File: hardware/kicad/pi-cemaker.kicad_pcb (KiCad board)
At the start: 4 copper layers, 85 x 56 mm, 4 parts

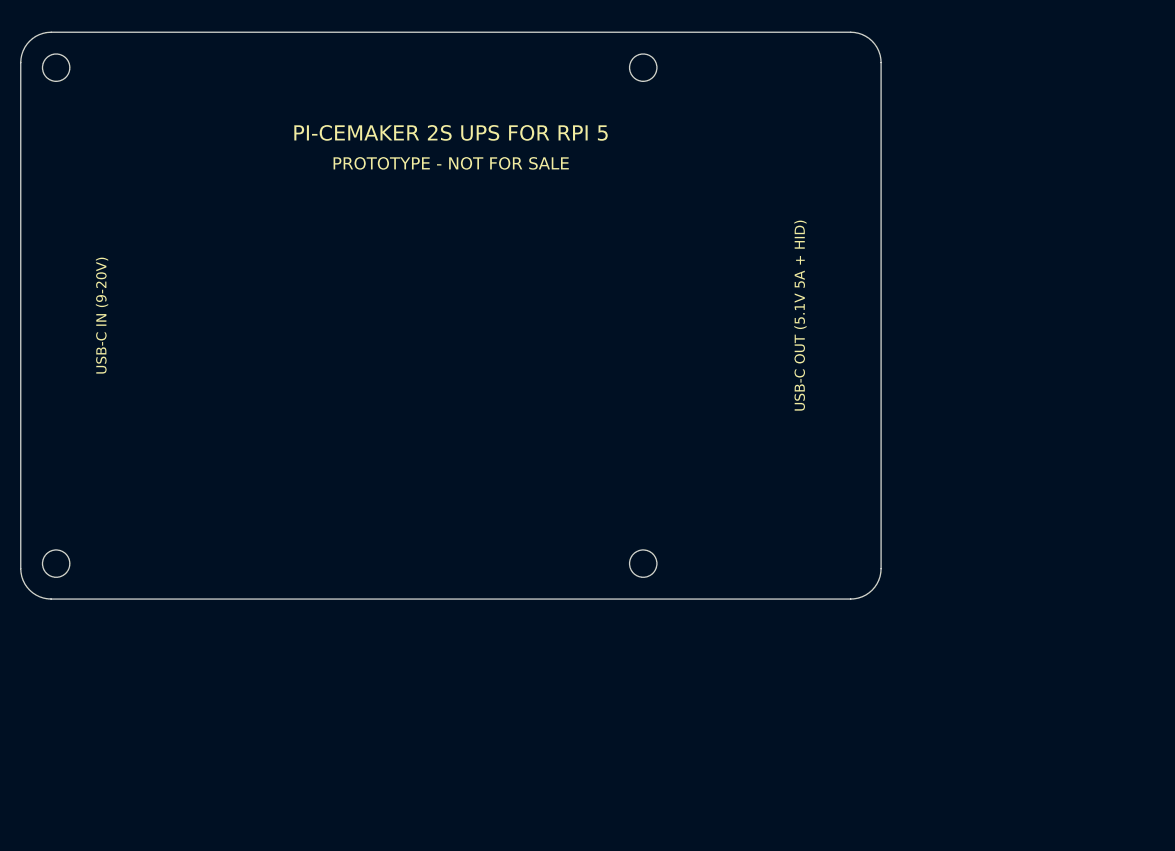
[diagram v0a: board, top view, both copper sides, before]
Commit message: hardware: draft Lite board generated from design.py (ERC clean, PCB unrouted/unreviewed)
Schematic (110 parts, ERC 0 violations), hand-built BQ25792 footprint,
placed + autorouted draft PCB (38 connections unrouted), draft BOM and a
decision log with a reversal path for each guess. No fab files produced.

Co-Authored-By: Claude Sonnet 5.5 <noreply@anthropic.com>
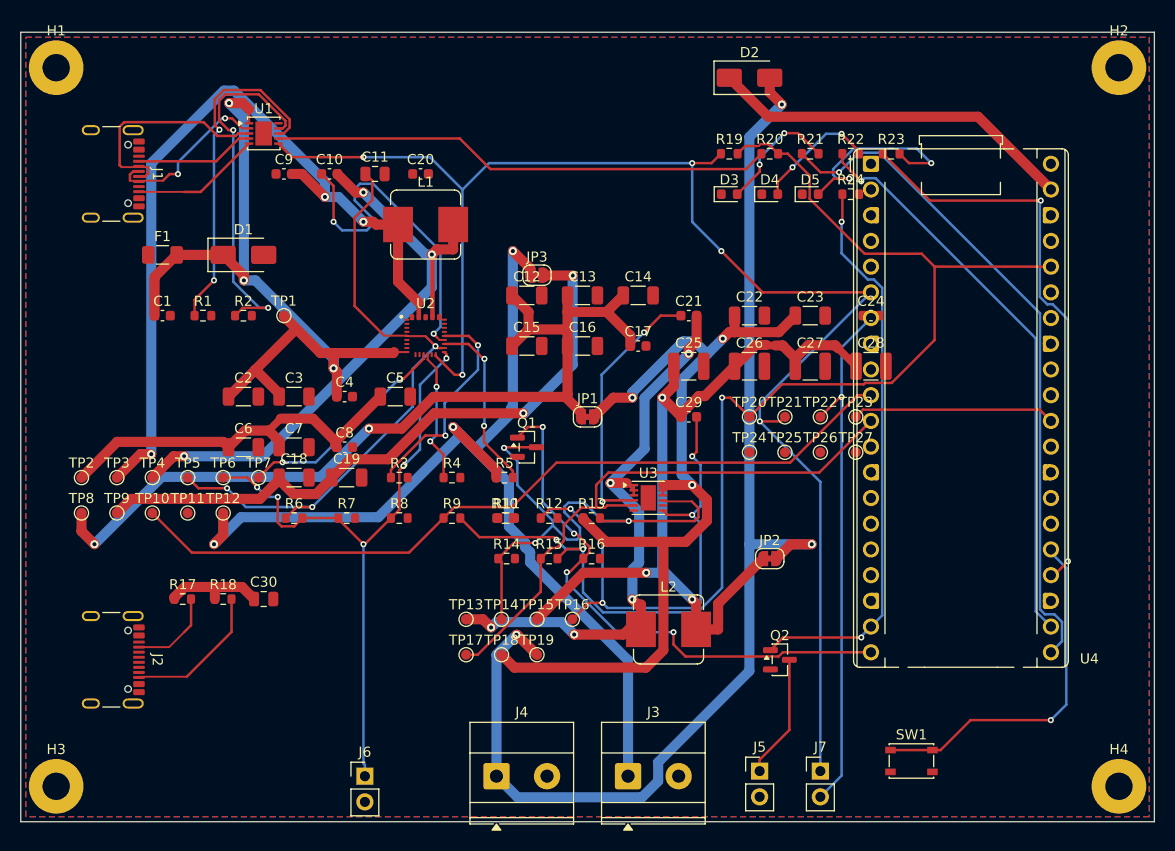
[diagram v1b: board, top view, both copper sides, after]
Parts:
- removed ? (x4): , MountingHole:MountingHole_2.7mm_M2.5
- added C1: 1uF 25V, C_0603_1608Metric, F.Cu at (14.0, 28.0)
- added C10: 47nF 25V, C_0603_1608Metric, F.Cu at (30.5, 14.0)
- added C11: 4.7uF 10V, C_0805_2012Metric, F.Cu at (35.0, 14.0)
- added C12: 10uF 25V, C_1206_3216Metric, F.Cu at (50.0, 26.0)
- added C13: 10uF 25V, C_1206_3216Metric, F.Cu at (55.5, 26.0)
- added C14: 10uF 25V, C_1206_3216Metric, F.Cu at (61.0, 26.0)
- added C15: 10uF 25V, C_1206_3216Metric, F.Cu at (50.0, 31.0)
- added C16: 10uF 25V, C_1206_3216Metric, F.Cu at (55.5, 31.0)
- added C17: 100nF 25V, C_0603_1608Metric, F.Cu at (61.0, 31.0)
- added C18: 10uF 16V, C_1206_3216Metric, F.Cu at (27.0, 44.0)
- added C19: 10uF 16V, C_1206_3216Metric, F.Cu at (32.2, 44.0)
- added C2: 10uF 25V, C_1206_3216Metric, F.Cu at (22.0, 36.0)
- added C20: 1nF 50V, C_0603_1608Metric, F.Cu at (39.5, 14.0)
- added C21: 100nF 16V, C_0603_1608Metric, F.Cu at (66.0, 28.0)
- added C22: 10uF 25V, C_1206_3216Metric, F.Cu at (72.0, 28.0)
- added C23: 10uF 25V, C_1206_3216Metric, F.Cu at (78.0, 28.0)
- added C24: 100nF 25V, C_0603_1608Metric, F.Cu at (84.0, 28.0)
- added C25: 33uF 16V, C_1210_3225Metric, F.Cu at (66.0, 33.0)
- added C26: 33uF 16V, C_1210_3225Metric, F.Cu at (72.0, 33.0)
- added C27: 33uF 16V (spare), C_1210_3225Metric, F.Cu at (78.0, 33.0)
- added C28: 33uF 16V (spare), C_1210_3225Metric, F.Cu at (84.0, 33.0)
- added C29: 33pF (CFF), C_0603_1608Metric, F.Cu at (66.0, 38.0)
- added C3: 10uF 25V, C_1206_3216Metric, F.Cu at (27.0, 36.0)
- added C30: 10uF 10V, C_0805_2012Metric, F.Cu at (24.0, 56.0)
- added C4: 100nF 25V, C_0603_1608Metric, F.Cu at (32.0, 36.0)
- added C5: 10uF 25V, C_1206_3216Metric, F.Cu at (37.0, 36.0)
- added C6: 10uF 25V, C_1206_3216Metric, F.Cu at (22.0, 41.0)
- added C7: 10uF 25V, C_1206_3216Metric, F.Cu at (27.0, 41.0)
- added C8: 100nF 25V, C_0603_1608Metric, F.Cu at (32.0, 41.0)
- added C9: 47nF 25V, C_0603_1608Metric, F.Cu at (26.0, 14.0)
- added D1: SMAJ13A, D_SMA, F.Cu at (22.0, 22.0)
- added D2: SS34, D_SMA, F.Cu at (72.0, 4.50)
- added D3: green, LED_0603_1608Metric, F.Cu at (70.0, 16.0)
- added D4: amber, LED_0603_1608Metric, F.Cu at (74.0, 16.0)
- added D5: red, LED_0603_1608Metric, F.Cu at (78.0, 16.0)
- added F1: 3.15A or 0R (fit one), Fuse_1206_3216Metric, F.Cu at (14.0, 22.0)
- added H1: M2.5, MountingHole_2.7mm_M2.5_Pad, F.Cu at (3.50, 3.50)
- added H2: M2.5, MountingHole_2.7mm_M2.5_Pad, F.Cu at (108.5, 3.50)
- added H3: M2.5, MountingHole_2.7mm_M2.5_Pad, F.Cu at (3.50, 74.5)
- added H4: M2.5, MountingHole_2.7mm_M2.5_Pad, F.Cu at (108.5, 74.5)
- added J1: USB-C in (PD sink), USB_C_Receptacle_GCT_USB4105-xx-A_16P_TopMnt_Horizontal, F.Cu at (8.00, 14.0)
- added J2: USB-C out to Pi 5 (power only), USB_C_Receptacle_GCT_USB4105-xx-A_16P_TopMnt_Horizontal, F.Cu at (8.00, 62.0)
- added J3: PACK+ / PACK- (off-board 2S BMS), TerminalBlock_Phoenix_MKDS-1,5-2_1x02_P5.00mm_Horizontal, F.Cu at (60.0, 73.5)
- added J4: 5V OUT / GND, TerminalBlock_Phoenix_MKDS-1,5-2_1x02_P5.00mm_Horizontal, F.Cu at (47.0, 73.5)
- added J5: To Pi 5 J2 power button, PinHeader_1x02_P2.54mm_Vertical, F.Cu at (73.0, 73.0)
- added J6: NTC (optional), PinHeader_1x02_P2.54mm_Vertical, F.Cu at (34.0, 73.5)
- added J7: I2C expansion (3V3 SDA), PinHeader_1x02_P2.54mm_Vertical, F.Cu at (79.0, 73.0)
- added JP1: VSYS link, SolderJumper-2_P1.3mm_Bridged_RoundedPad1.0x1.5mm, F.Cu at (56.0, 38.0)
- added JP2: 5V link, SolderJumper-2_P1.3mm_Bridged_RoundedPad1.0x1.5mm, F.Cu at (74.0, 52.0)
- added JP3: PACK link, SolderJumper-2_P1.3mm_Bridged_RoundedPad1.0x1.5mm, F.Cu at (51.0, 24.0)
- added L1: 1uH >=8A sat, L_Bourns_SRP7028A_7.3x6.6mm, F.Cu at (40.0, 19.0)
- added L2: 4.7uH >=8A sat, L_Bourns_SRP7028A_7.3x6.6mm, F.Cu at (64.0, 59.0)
- added Q1: 2N7002, SOT-23, F.Cu at (50.0, 41.0)
- added Q2: 2N7002, SOT-23, F.Cu at (75.0, 62.0)
- added R1: 10k (12 V), R_0603_1608Metric, F.Cu at (18.0, 28.0)
- added R10: 10k, R_0603_1608Metric, F.Cu at (47.8, 48.0)
- added R11: 102k (FBT), R_0603_1608Metric, F.Cu at (48.0, 48.0)
- added R12: 19.1k (FBB), R_0603_1608Metric, F.Cu at (52.2, 48.0)
- added R13: 62k (ENT), R_0603_1608Metric, F.Cu at (56.4, 48.0)
- added R14: 21.5k (ENB), R_0603_1608Metric, F.Cu at (48.0, 52.0)
- added R15: 10k, R_0603_1608Metric, F.Cu at (52.2, 52.0)
- added R16: 100k (gate pull-down), R_0603_1608Metric, F.Cu at (56.4, 52.0)
- added R17: 10k (Rp, 3 A), R_0603_1608Metric, F.Cu at (16.0, 56.0)
- added R18: 10k (Rp, 3 A), R_0603_1608Metric, F.Cu at (20.0, 56.0)
- added R19: 10k, R_0603_1608Metric, F.Cu at (70.0, 12.0)
- added R2: 22.6k (3 A), R_0603_1608Metric, F.Cu at (22.0, 28.0)
- added R20: 10k, R_0603_1608Metric, F.Cu at (74.0, 12.0)
- added R21: 1k, R_0603_1608Metric, F.Cu at (78.0, 12.0)
- added R22: 1k, R_0603_1608Metric, F.Cu at (82.0, 12.0)
- added R23: 1k, R_0603_1608Metric, F.Cu at (86.0, 12.0)
- added R24: 100k (gate pull-down), R_0603_1608Metric, F.Cu at (82.0, 16.0)
- added R3: 6.04k 1% (2S,1.5MHz), R_0603_1608Metric, F.Cu at (37.4, 44.0)
- added R4: 10k (CE low = charge on), R_0603_1608Metric, F.Cu at (42.6, 44.0)
- added R5: 100R, R_0603_1608Metric, F.Cu at (47.8, 44.0)
- added R6: 5.24k (RT1), R_0603_1608Metric, F.Cu at (27.0, 48.0)
- added R7: 30.31k (RT2), R_0603_1608Metric, F.Cu at (32.2, 48.0)
- added R8: 10k fixed NTC stand-in, R_0603_1608Metric, F.Cu at (37.4, 48.0)
- added R9: 10k, R_0603_1608Metric, F.Cu at (42.6, 48.0)
- added SW1: USER, SW_SPST_PTS810, F.Cu at (88.0, 72.0)
- added TP1: VBUS, TestPoint_Pad_D1.0mm, F.Cu at (26.0, 28.0)
- added TP10: STAT, TestPoint_Pad_D1.0mm, F.Cu at (13.0, 47.5)
- added TP11: INT, TestPoint_Pad_D1.0mm, F.Cu at (16.5, 47.5)
- added TP12: PACK_P, TestPoint_Pad_D1.0mm, F.Cu at (20.0, 47.5)
- added TP13: SW_B, TestPoint_Pad_D1.0mm, F.Cu at (44.0, 58.0)
- added TP14: EN_B, TestPoint_Pad_D1.0mm, F.Cu at (47.5, 58.0)
- added TP15: V5_B, TestPoint_Pad_D1.0mm, F.Cu at (51.0, 58.0)
- added TP16: FB, TestPoint_Pad_D1.0mm, F.Cu at (54.5, 58.0)
- added TP17: PG, TestPoint_Pad_D1.0mm, F.Cu at (44.0, 61.5)
- added TP18: VSYS_B, TestPoint_Pad_D1.0mm, F.Cu at (47.5, 61.5)
- added TP19: V5, TestPoint_Pad_D1.0mm, F.Cu at (51.0, 61.5)
- added TP2: PMID, TestPoint_Pad_D1.0mm, F.Cu at (6.00, 44.0)
- added TP20: +3V3, TestPoint_Pad_D1.0mm, F.Cu at (72.0, 38.0)
- added TP21: SDA, TestPoint_Pad_D1.0mm, F.Cu at (75.5, 38.0)
- added TP22: SCL, TestPoint_Pad_D1.0mm, F.Cu at (79.0, 38.0)
- added TP23: RUN, TestPoint_Pad_D1.0mm, F.Cu at (82.5, 38.0)
- added TP24: GND, TestPoint_Pad_D1.0mm, F.Cu at (72.0, 41.5)
- added TP25: GND, TestPoint_Pad_D1.0mm, F.Cu at (75.5, 41.5)
- added TP26: GND, TestPoint_Pad_D1.0mm, F.Cu at (79.0, 41.5)
- added TP27: GND, TestPoint_Pad_D1.0mm, F.Cu at (82.5, 41.5)
- added TP3: SW1, TestPoint_Pad_D1.0mm, F.Cu at (9.50, 44.0)
- added TP4: SW2, TestPoint_Pad_D1.0mm, F.Cu at (13.0, 44.0)
- added TP5: REGN, TestPoint_Pad_D1.0mm, F.Cu at (16.5, 44.0)
- added TP6: TS, TestPoint_Pad_D1.0mm, F.Cu at (20.0, 44.0)
- added TP7: QON, TestPoint_Pad_D1.0mm, F.Cu at (23.5, 44.0)
- added TP8: VSYS, TestPoint_Pad_D1.0mm, F.Cu at (6.00, 47.5)
- added TP9: BAT, TestPoint_Pad_D1.0mm, F.Cu at (9.50, 47.5)
- added U1: HUSB238, DFN-10-1EP_3x3mm_P0.5mm_EP1.65x2.38mm, F.Cu at (24.0, 10.0)
- added U2: BQ25792, VQFN-HR-29_RQM0029A_4x4mm, F.Cu at (40.0, 30.0)
- added U3: LMR51450SDRRR, WSON-12-1EP_3x3mm_P0.5mm_EP1.5x2.5mm, F.Cu at (62.0, 46.0)
- added U4: Raspberry Pi Pico (RP2040), RaspberryPi_Pico_Common_THT, F.Cu at (84.0, 13.0)
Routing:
- net SDA: track 0.00 -> 152.3 mm, vias 0 -> 5
- net V5: track 0.00 -> 130.6 mm, vias 0 -> 3
- net +3V3: track 0.00 -> 124.8 mm, vias 0 -> 3
- net PACK_P: track 0.00 -> 105.0 mm, vias 0 -> 3
- net SCL: track 0.00 -> 101.9 mm, vias 0 -> 1
- net VSYS_B: track 0.00 -> 91.5 mm, vias 0 -> 3
- net VSYS: track 0.00 -> 89.6 mm, vias 0 -> 2
- net SW1: track 0.00 -> 81.0 mm, vias 0 -> 3
- net VBUS: track 0.00 -> 80.9 mm, vias 0 -> 3
- net STAT: track 0.00 -> 79.1 mm
- net V5_B: track 0.00 -> 79.0 mm, vias 0 -> 3
- net LED_PWR: track 0.00 -> 67.1 mm, vias 0 -> 1
- net TS: track 0.00 -> 64.3 mm, vias 0 -> 5
- net BAT: track 0.00 -> 64.2 mm, vias 0 -> 2
- net SW2: track 0.00 -> 62.3 mm, vias 0 -> 3
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- added copper zone on B.Cu, net GND
- added copper zone on F.Cu, net GND
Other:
- board size 85 x 56 mm -> 112 x 78 mm
- copper layers 4 -> 2
- rule pad_to_mask_clearance: 0.05 -> 0
- board text removed: "PI-CEMAKER 2S UPS FOR RPI 5"
- board text removed: "PROTOTYPE - NOT FOR SALE"
- board text removed: "USB-C IN (9-20V)"
- board text removed: "USB-C OUT (5.1V 5A + HID)"
